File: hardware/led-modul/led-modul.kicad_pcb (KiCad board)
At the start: 4 copper layers, 68 x 86.5 mm, 170 parts, among them J1 DEBUG, J2 BUS_IN, J201 24V IN 20A, J202 BLOKK 1, J203 BLOKK 2, J204 BLOKK 3, J3 BUS_OUT, J4 BŐVÍTŐ, Q201 NTMFS5C604NL, Q202 NTD5C648NL, Q203 NTD5C648NL, Q204 NTD5C648NL, Q205 NTD5C648NL, Q206 NTD5C648NL, Q207 NTD5C648NL, U2 TCAN1044AVDRQ1, U201 UCC27524DR, U202 UCC27524DR, U203 UCC27524DR, U204 LM74700-Q1, U205 MC78L12ACDR2G, U206 INA181A2IDBVR, U3 ESD2CAN24-Q1, U5 AP2112K-3.3TRG1, U6 STM32F303RET6, Y1 8MHz

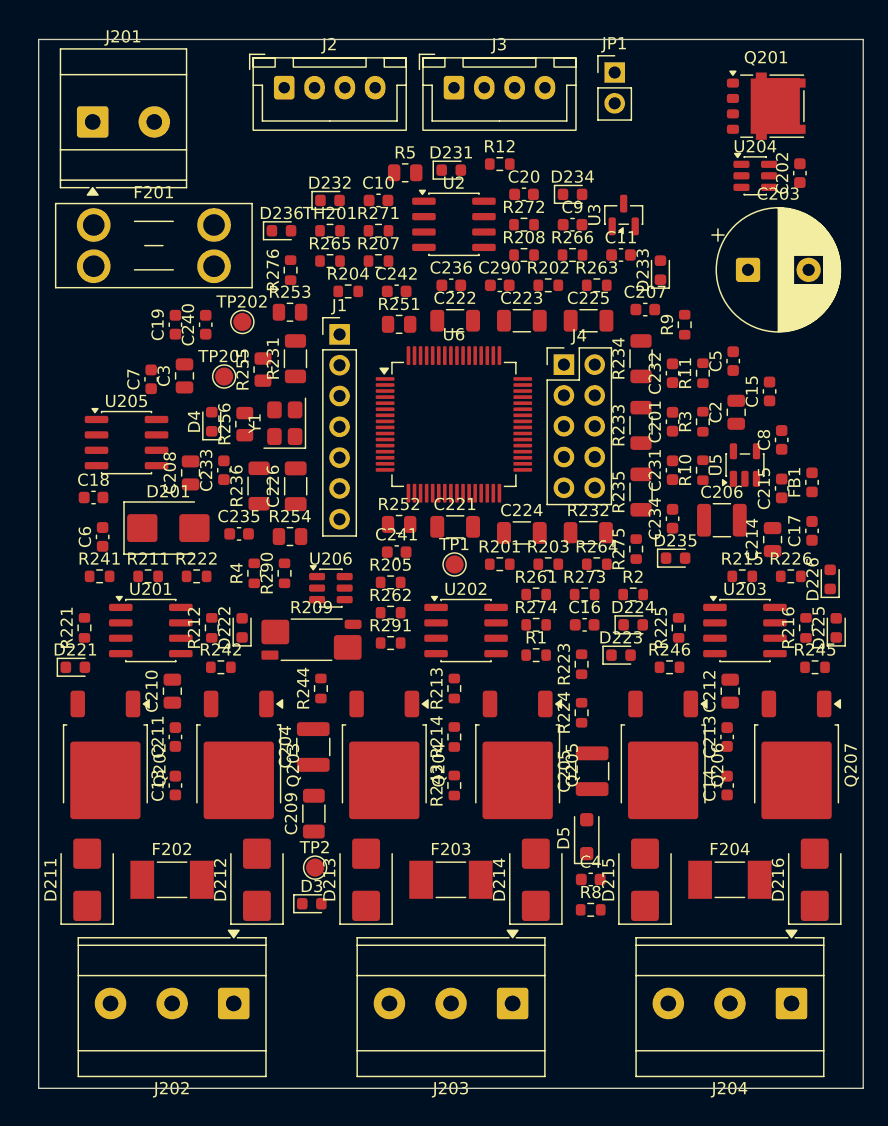
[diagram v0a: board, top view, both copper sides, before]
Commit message: Hardver: szakértői javítások (D74–D77), STM32L433 + SN65HVD230 + GND-ági polaritásvédelem (D78–D81), teljes ellenőrzés
- D74–D77: busz-GND ellenállás, CAN-fojtó-hely, TVS a +5V_BUCK-on és a VUSB-n, bemenetvédelem,
  230 V-os és antenna-tiltás a NYÁK-on, SCT-jack footprint
- D78–D80: modul-MCU STM32L433RCT3 (VIN_SENSE PB1, LED: TIM15/TIM16, I_SENSE PA3), modul-transceiver
  SN65HVD230, N-FET a GND-ágban (vezérlő Q1, LED Q201, relé Q100), MCP9701A, táp-LED a +5V-ról,
  2 oz a LED-/relémodulon, AP2112K marad; D81 javaslat (TPD4E02B04 a bemeneteken)
- CubeMX-projektek L433-ra, fejsoros kódgenerálással ellenőrizve (minden periféria inicializálódik)
- gen/ellenorzes.py (ERC, láb ↔ pad, modulmag, CubeMX, polaritásvédelem, NYÁK ↔ rajz, DRC) – 0 hiba
- gen/bom.sh + bom/*.csv darabjegyzék; docs/komponenslista.md a konzulensnek
- kontextus: DONTESEK D74–D81, specifikációk, ATTEKINTES, NAPLO, beszerzési lista; alkatrészkészlet-jegyzet (claude.ai)

Co-Authored-By: Claude Opus 5.5 <noreply@anthropic.com>
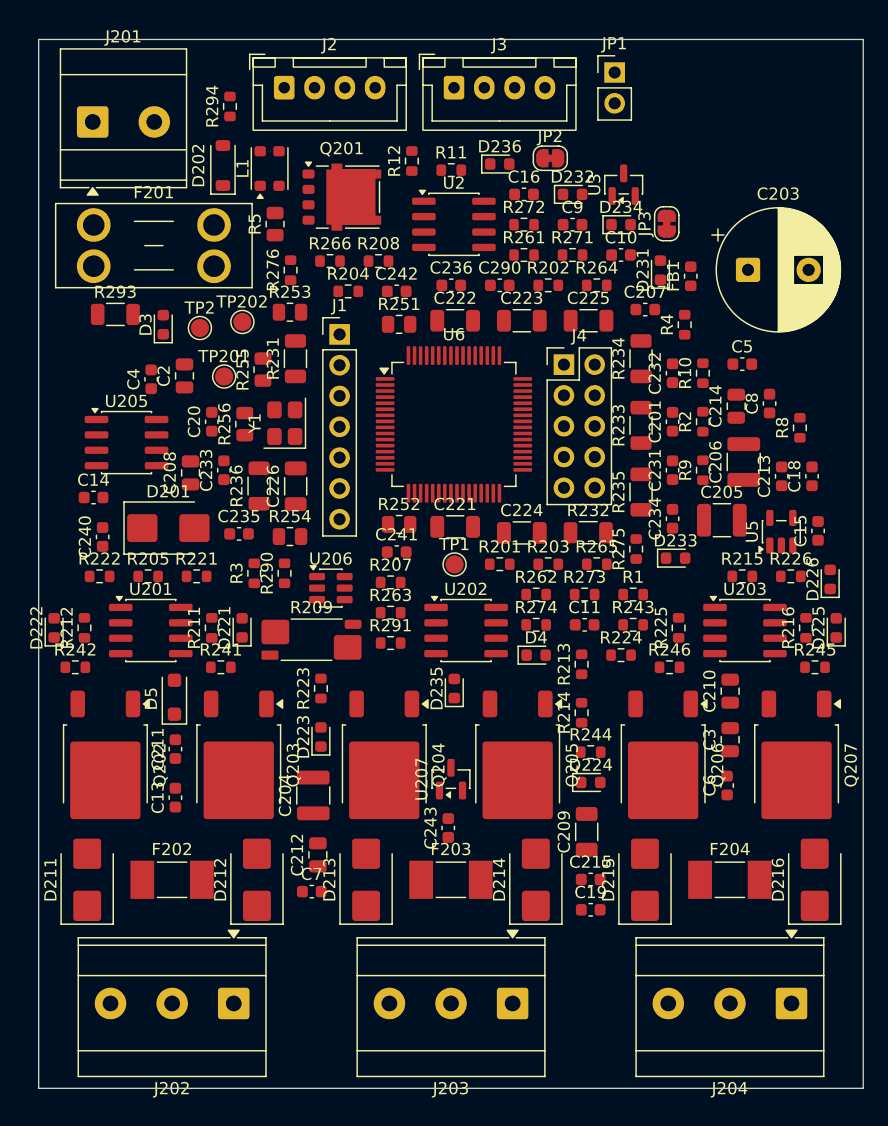
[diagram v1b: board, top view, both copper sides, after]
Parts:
- removed C17, C202: 100n, Capacitor_SMD:C_0603_1608Metric
- removed TH201: 10k B3435, Resistor_SMD:R_0603_1608Metric
- removed U204: LM74700-Q1, Package_TO_SOT_SMD:SOT-23-6
- added C243: 100n, Capacitor_SMD:C_0603_1608Metric, F.Cu at (133.8, 165.0)
- added D202: BZT52C15, Diode_SMD:D_SOD-123, F.Cu at (115.2, 110.4)
- added JP2: áthidaló, Jumper:SolderJumper-2_P1.3mm_Bridged_RoundedPad1.0x1.5mm, F.Cu at (142.2, 109.8)
- added JP3: áthidaló, Jumper:SolderJumper-2_P1.3mm_Bridged_RoundedPad1.0x1.5mm, F.Cu at (151.8, 115.2)
- added L1: DNP, Inductor_SMD:L_CommonModeChoke_Coilank_ACM3225, F.Cu at (119.0, 110.6)
- added R293: 1R, Resistor_SMD:R_1206_3216Metric, F.Cu at (106.3, 122.7)
- added R294: 10k, Resistor_SMD:R_0603_1608Metric, F.Cu at (115.8, 105.5)
- added U207: MCP9701AT-E/TT, Package_TO_SOT_SMD:SOT-23, F.Cu at (134.0, 161.0)
- R208: value 10k 1% -> 200R
- R241, R242, R243, R244, R245, R246: value 4k7 -> 10k
- U2: value TCAN1044AVDRQ1 -> SN65HVD230D
- U6: value STM32F303RET6 -> STM32L433RCT3
- moved C18 59.3 mm to (163.8, 136.0), turned to 90 degrees
- moved C19 59.2 mm to (145.5, 171.8), turned to 0 degrees
- moved C14 57.4 mm to (104.5, 137.8), turned to 0 degrees
- moved C6 55.4 mm to (156.8, 161.5)
- moved C4 54.9 mm to (109.3, 128.0), turned to 90 degrees
- moved C3 54.1 mm to (157.0, 157.7)
- moved D3 49.3 mm to (110.3, 123.5), turned to 90 degrees
- moved C210 46.0 mm to (157.0, 153.7)
- moved C2 45.6 mm to (112.0, 127.7)
- moved TP2 45.5 mm to (113.3, 123.8)
- moved C7 44.3 mm to (122.5, 170.3), turned to 0 degrees
- moved R8 43.3 mm to (162.8, 132.0), turned to 90 degrees
- moved R4 41.0 mm to (153.3, 123.5)
- moved R3 39.1 mm to (117.8, 144.0)
- moved C212 36.6 mm to (123.0, 167.2)
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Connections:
- net /NTC renamed /T_SENSE
- C18 pad 1: +5V -> +3V3
- C19 pad 1: +5V -> +3V3
- F201 pad 2: /+24V_F -> /+24V_RAIL
- J2 pad 2: GND -> /GND_BUS
- J201 pad 2: GND -> /GND_IN
- J3 pad 2: GND -> /GND_BUS
- Q201 pad 1: /+24V_F -> GND
- Q201 pad 2: /+24V_F -> GND
- Q201 pad 3: /+24V_F -> GND
- Q201 pad 5: /+24V_RAIL -> /GND_IN
- R208 pad 1: +3V3 -> Net-(U207-V_{OUT})
- R8 pad 1: +3V3 -> +5V
- U2 pad 3: +5V -> +3V3
- U2 pad 5: +3V3 -> unconnected-(U2-Vref-Pad5)
- U2 pad 6: /modulmag/CAN_L -> /modulmag/CAN_L_T
- U2 pad 7: /modulmag/CAN_H -> /modulmag/CAN_H_T
- U6 pad 17: /DS4 -> /I_SENSE
- U6 pad 23: /I_SENSE -> /DS4
- U6 pad 27: unconnected-(U6-PB1-Pad27) -> /VIN_SENSE
- U6 pad 30: /VIN_SENSE -> /modulmag/PB11
- U6 pad 35: /modulmag/PB14 -> /CH4_PWM
- U6 pad 36: /modulmag/PB15 -> /CH5_PWM
- U6 pad 37: /CH4_PWM -> unconnected-(U6-PC6-Pad37)
- U6 pad 38: /CH5_PWM -> unconnected-(U6-PC7-Pad38)
- U6 pad 39: /CH6_PWM -> unconnected-(U6-PC8-Pad39)
- U6 pad 61: /modulmag/PB8 -> /CH6_PWM

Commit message: Hardver: determinisztikus UUID-k – a NYÁK-footprintek újra a rajzi szimbólumokra mutatnak
- kigen: a szimbólum-UUID a projekt + hivatkozási jel alapján (uuid5), a többi elemé laponként sorszámból –
  két generálás bájtra azonos fájlt ad, és az újragenerálás nem töri el a „Update PCB from Schematic”-ot (D67)
- a négy NYÁK újragenerálva: mind a 581 footprint a saját szimbólumára mutat (előtte egy sem)
- ellenorzes.py: új ellenőrzés a NYÁK ↔ rajz szimbólum-kapcsolatra; teljes futás: 0 hiba
- README, NAPLO

Co-Authored-By: Claude Opus 5.5 <noreply@anthropic.com>
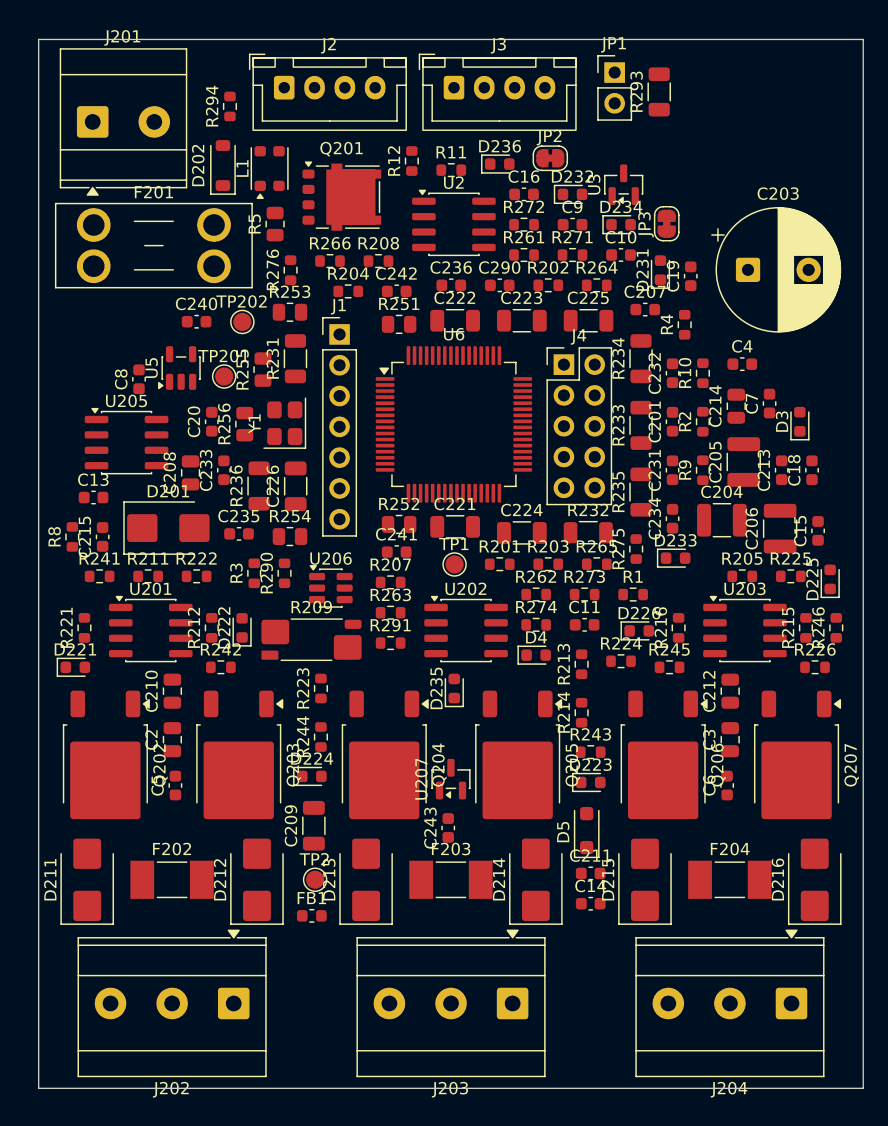
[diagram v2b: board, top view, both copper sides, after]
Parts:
- moved FB1 61.3 mm to (122.5, 172.3), turned to 0 degrees
- moved R8 60.7 mm to (102.8, 141.0)
- moved C5 58.3 mm to (111.3, 161.5), turned to 90 degrees
- moved C7 55.2 mm to (160.3, 130.0), turned to 90 degrees
- moved D3 53.1 mm to (162.8, 131.5)
- moved C14 52.9 mm to (145.5, 171.3)
- moved C19 52.9 mm to (153.8, 119.5), turned to 90 degrees
- moved C8 52.0 mm to (108.3, 128.0)
- moved U5 51.3 mm to (111.7, 127.1)
- moved C215 49.2 mm to (105.3, 141.0), turned to 90 degrees
- moved R205 49.0 mm to (158.0, 144.3)
- moved C4 48.8 mm to (158.0, 126.8), turned to 0 degrees
- moved R293 48.5 mm to (151.2, 104.3), turned to 90 degrees
- moved TP2 46.5 mm to (122.8, 169.3)
- moved C210 46.0 mm to (111.0, 153.7)
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
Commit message: Hardver: 1 oz + fedetlen nagyáramú sávok (D82), reprodukálható rajzgenerálás; kontextus: rajzlezárás
- D82: minden NYÁK 1 oz (a JLC 2 oz-nál ≥ 0,2 mm szélességet/távolságot kér, az LQFP-64 rése épp ennyi);
  a nagyáramú sávok fedetlenek, utólag ónozva / vezetékkel – leírás a NYAK-ELOKESZITES-ben (a söntöt nem ónozni)
- LED- és relé-NYÁK újragenerálva 1 oz-zal; az ellenőrző az 1 oz-ot figyeli
- kigen: minden egységpéldány a szimbólum összes lábát felsorolja → a „sch upgrade” nem pótol véletlen UUID-t,
  mind az öt rajz bájtra reprodukálható
- kontextus: ATTEKINTES (rajzok lezárva 10-22), UTEMTERV, NAPLO, DONTESEK D82; komponenslista állapotsora

Co-Authored-By: Claude Opus 5.5 <noreply@anthropic.com>
Claude-Session: https://claude.ai/code/session_01KVtZMUPbtveTXy9VyJshyt
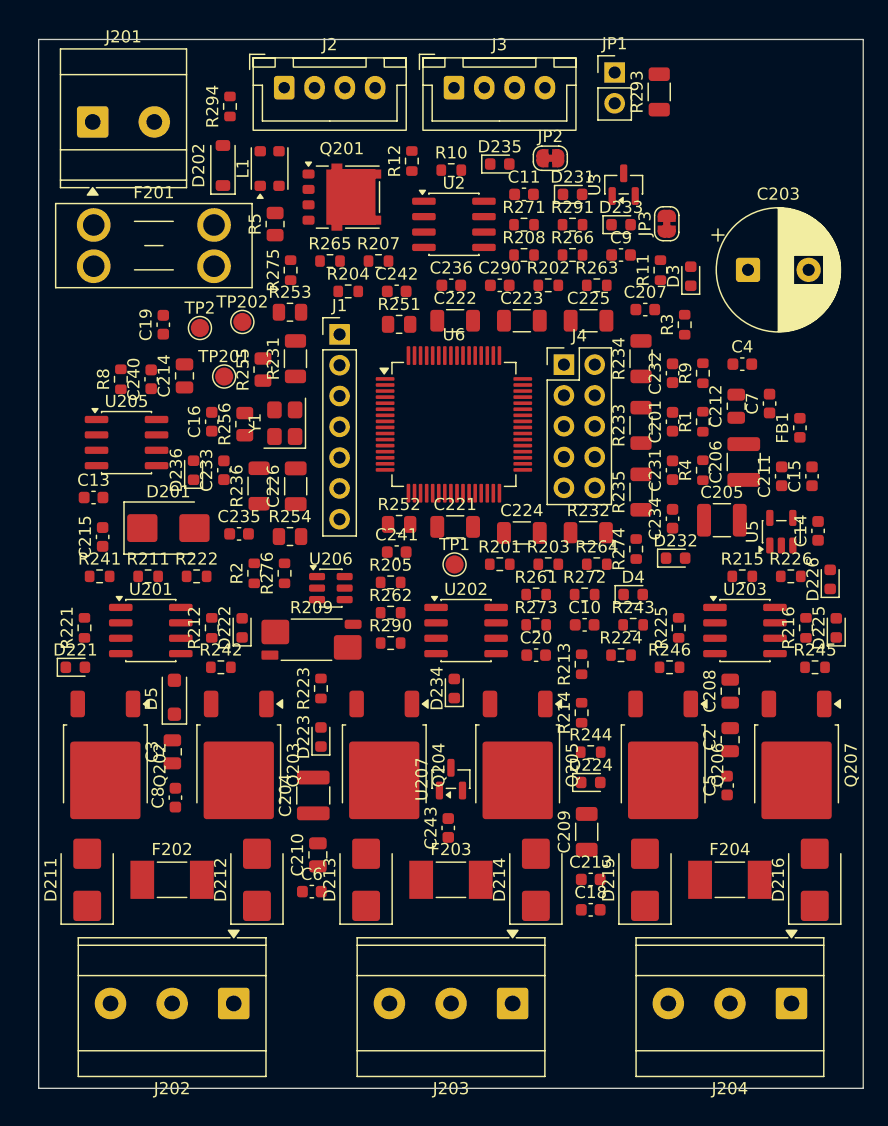
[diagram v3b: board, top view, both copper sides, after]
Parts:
- moved FB1 56.9 mm to (162.8, 132.0), turned to 90 degrees
- moved U5 51.3 mm to (161.2, 140.6)
- moved C208 48.0 mm to (157.0, 153.7)
- moved TP2 46.5 mm to (113.3, 123.8)
- moved C3 46.0 mm to (111.0, 158.7)
- moved C2 46.0 mm to (157.0, 157.7)
- moved C214 45.6 mm to (112.0, 127.7)
- moved C5 45.5 mm to (156.8, 161.5)
- moved C19 43.7 mm to (110.3, 123.5)
- moved D235 43.4 mm to (138.0, 110.3), turned to 0 degrees
- moved R3 41.0 mm to (153.3, 123.5)
- moved D234 40.6 mm to (134.3, 153.5), turned to 90 degrees
- moved C204 40.6 mm to (122.6, 162.3), turned to 90 degrees
- moved C18 40.6 mm to (145.5, 171.8), turned to 0 degrees
- moved R2 39.1 mm to (117.8, 144.0)
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
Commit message: Hardver: legolcsóbb beszerzés (D84) – Hestore + DigiKey, a rajz a kapható típusokra igazítva; beszerzési lista
- gen/beszerzes.py → bom/beszerzes.csv: BOM-tételenként forrás, Hestore-kód, nettó ár, készlet
- J1/J100 Degson DG250, J201 DG128 (15 A), J202–J204 KF128, F201 15 A; L1/L3 HPI0630 (saját footprint);
  R209 CRE2512; C40/C41 12 pF; ESP32-C6-WROOM-1-N8; SS56C, BAT54HT1G, STPS3L60U, BLM18EG221
- NYÁK-ok újragenerálva (a layout még nem indult el); bekötés változatlan, ellenorzes.py: 0 hiba
- SAMPLE-KERESEK: az NTMFS5C604NL nincs kézben (javítva)

Co-Authored-By: Claude Opus 5.5 <noreply@anthropic.com>
Claude-Session: https://claude.ai/code/session_01KVtZMUPbtveTXy9VyJshyt
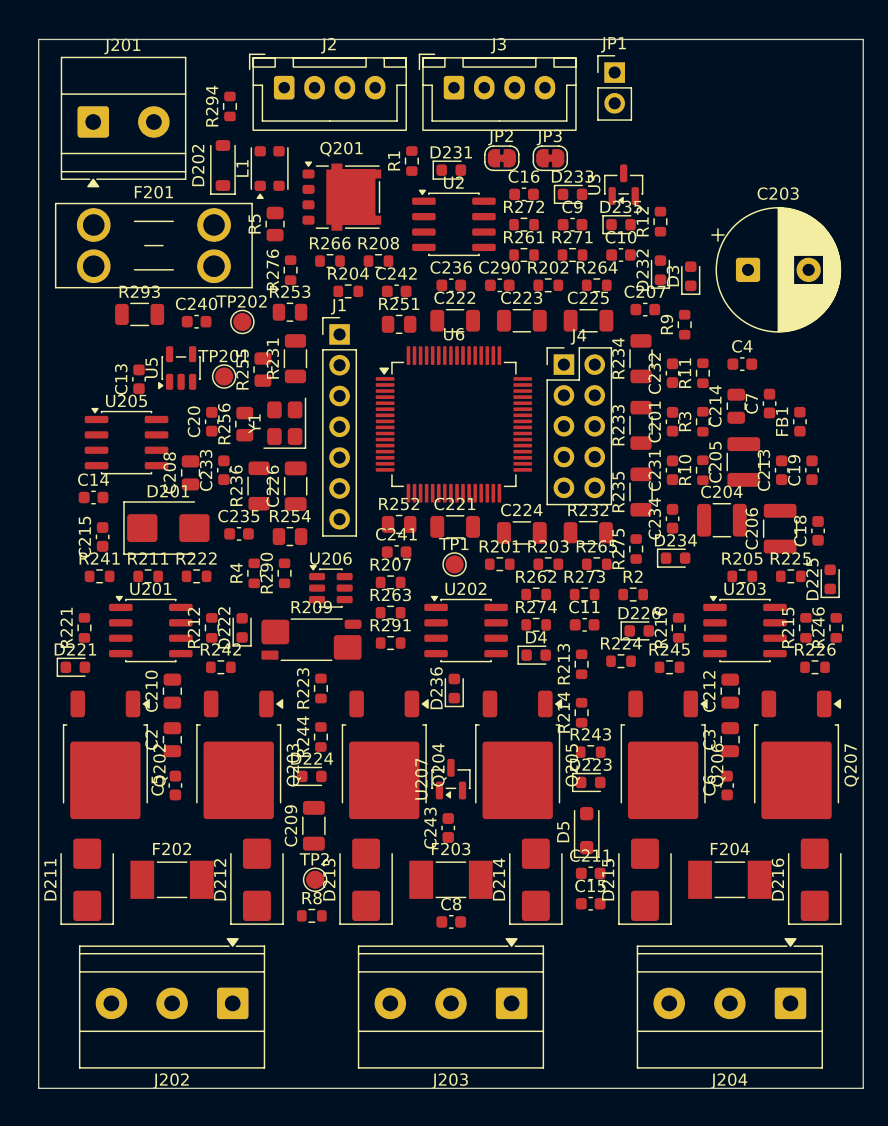
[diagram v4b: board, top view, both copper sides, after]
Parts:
- D211, D212, D213, D214, D215, D216: value B360B -> STPS3L60U
- F201: value 20A -> 15A
- FB1: value ferrit ≤0,1Ω -> BLM18EG221
- J201: value 24V IN 20A -> 24V IN 15A; footprint TerminalBlock_Phoenix:TerminalBlock_Phoenix_MKDS-3-2-5.08_1x02_P5.08mm_Horizontal -> TerminalBlock_Phoenix:TerminalBlock_Phoenix_MKDS-1,5-2_1x02_P5.00mm_Horizontal
- J202, J203, J204: footprint TerminalBlock_Phoenix:TerminalBlock_Phoenix_MKDS-3-3-5.08_1x03_P5.08mm_Horizontal -> TerminalBlock_Phoenix:TerminalBlock_Phoenix_MKDS-1,5-3_1x03_P5.00mm_Horizontal
- moved C14 59.8 mm to (104.5, 137.8), turned to 0 degrees
- moved C19 54.8 mm to (163.8, 135.5)
- moved U5 51.3 mm to (111.7, 127.1)
- moved C208 48.0 mm to (112.5, 135.7)
- moved R8 47.0 mm to (122.5, 172.3), turned to 0 degrees
- moved R293 46.6 mm to (108.3, 122.7), turned to 0 degrees
- moved TP2 46.5 mm to (122.8, 169.3)
- moved C3 46.0 mm to (157.0, 157.7)
- moved C2 46.0 mm to (111.0, 157.7)
- moved C214 45.6 mm to (157.5, 130.2)
- moved C5 45.5 mm to (111.3, 161.5)
- moved C204 40.6 mm to (156.3, 139.6), turned to 0 degrees
- moved C15 39.7 mm to (145.5, 171.3), turned to 0 degrees
- moved R4 38.0 mm to (117.8, 144.0)
- moved R291 37.6 mm to (129.0, 149.8)
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
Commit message: Hardver: legolcsóbb beszerzés LCSC-ről (D85), megszűnt FET-ek pótlása, LCSC-kosárlista
- gen/lcsc.py: LCSC-árak a JLC alkatrészkeresőjéből; gen/beszerzes.py soronként a legolcsóbb forrás (Hestore / LCSC, ÁFA-val)
- bom/lcsc-kosar.csv: 99 tétel (~15 eFt), az LCSC BOM Tooljába feltölthető; házak később, ST-Link/Nucleo kézben
- Q202–Q207 NTD5C648NL → NCE6080K, Q201 NTMFS5C604NL → NCEP6090AGU (nem kaphatók), F201 → NANO² 15 A,
  D211–D216 SS56B, J1/J100 DG128, L1/L3 LCSC-s 0630-as tekercs, kis ESR-ű kvarcok
- bekötés változatlan (netlista 0 / 0), ellenorzes.py: 0 hiba

Co-Authored-By: Claude Opus 5.5 <noreply@anthropic.com>
Claude-Session: https://claude.ai/code/session_01KVtZMUPbtveTXy9VyJshyt
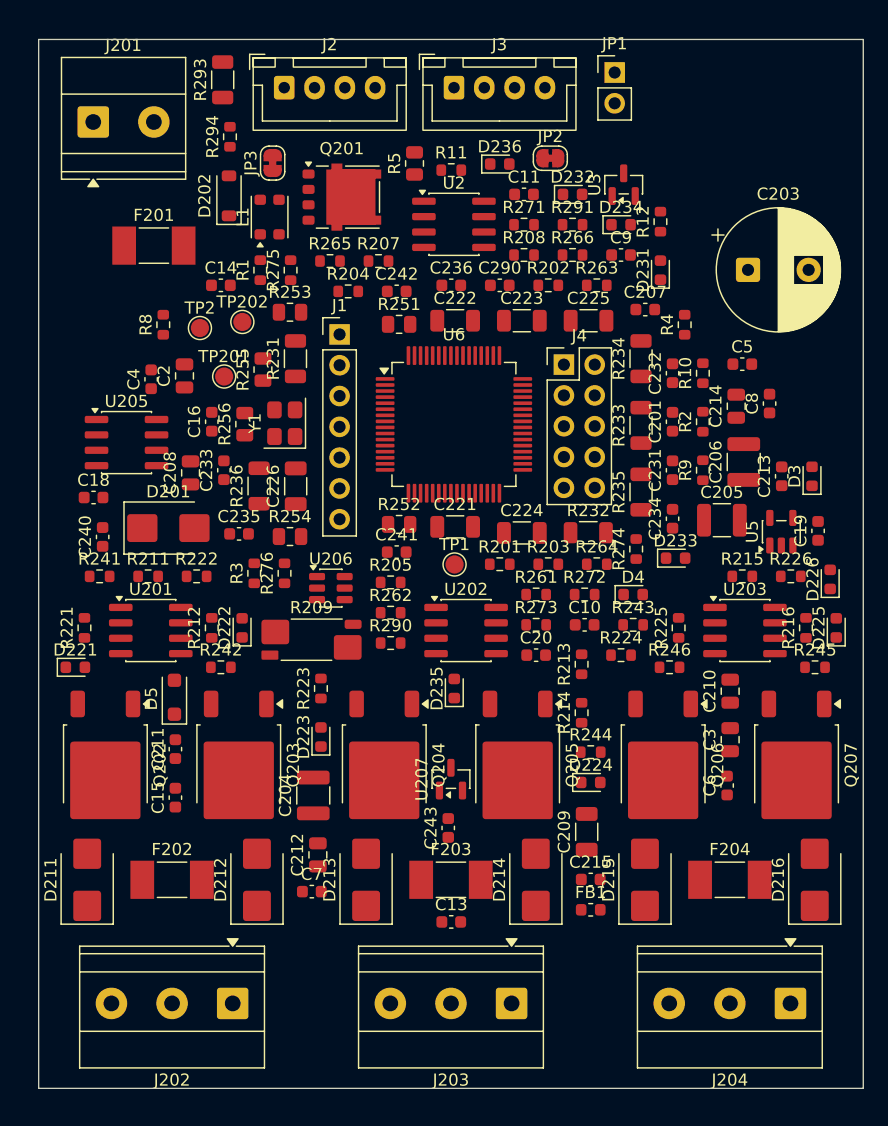
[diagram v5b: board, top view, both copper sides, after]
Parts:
- D211, D212, D213, D214, D215, D216: value STPS3L60U -> SS56B
- F201: footprint Fuse:Fuseholder_Blade_Mini_Keystone_3568 -> Fuse:Fuse_Littelfuse-NANO2-451_453
- Q201: value NTMFS5C604NL -> NCEP6090AGU
- Q202, Q203, Q204, Q205, Q206, Q207: value NTD5C648NL -> NCE6080K
- moved C18 59.8 mm to (104.5, 137.8), turned to 0 degrees
- moved C5 58.3 mm to (158.0, 126.8), turned to 0 degrees
- moved C7 55.2 mm to (122.5, 170.3), turned to 0 degrees
- moved C13 51.6 mm to (134.0, 172.8), turned to 0 degrees
- moved U5 51.3 mm to (161.2, 140.6)
- moved R8 50.3 mm to (110.3, 123.5), turned to 90 degrees
- moved C8 50.2 mm to (160.3, 130.0), turned to 90 degrees
- moved C215 49.2 mm to (145.5, 169.3), turned to 0 degrees
- moved C4 48.8 mm to (109.3, 128.0), turned to 90 degrees
- moved TP2 46.5 mm to (113.3, 123.8)
- moved C210 46.0 mm to (157.0, 153.7)
- moved FB1 43.8 mm to (145.5, 171.8), turned to 0 degrees
- moved D236 43.4 mm to (138.0, 110.3), turned to 0 degrees
- moved R4 41.0 mm to (153.3, 123.5)
- moved D235 40.6 mm to (134.3, 153.5), turned to 90 degrees
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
